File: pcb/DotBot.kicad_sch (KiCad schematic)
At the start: 65 parts, among them J1 Shield Header, J10 Extra Pins, J11 Motor connector, J12 Motor connector, J6 SWD, J7 Shield Header, J8 Extra Pins, J9 Extra Pins, Q1 DMN62D0U-7, Q2 DMG2301L-7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

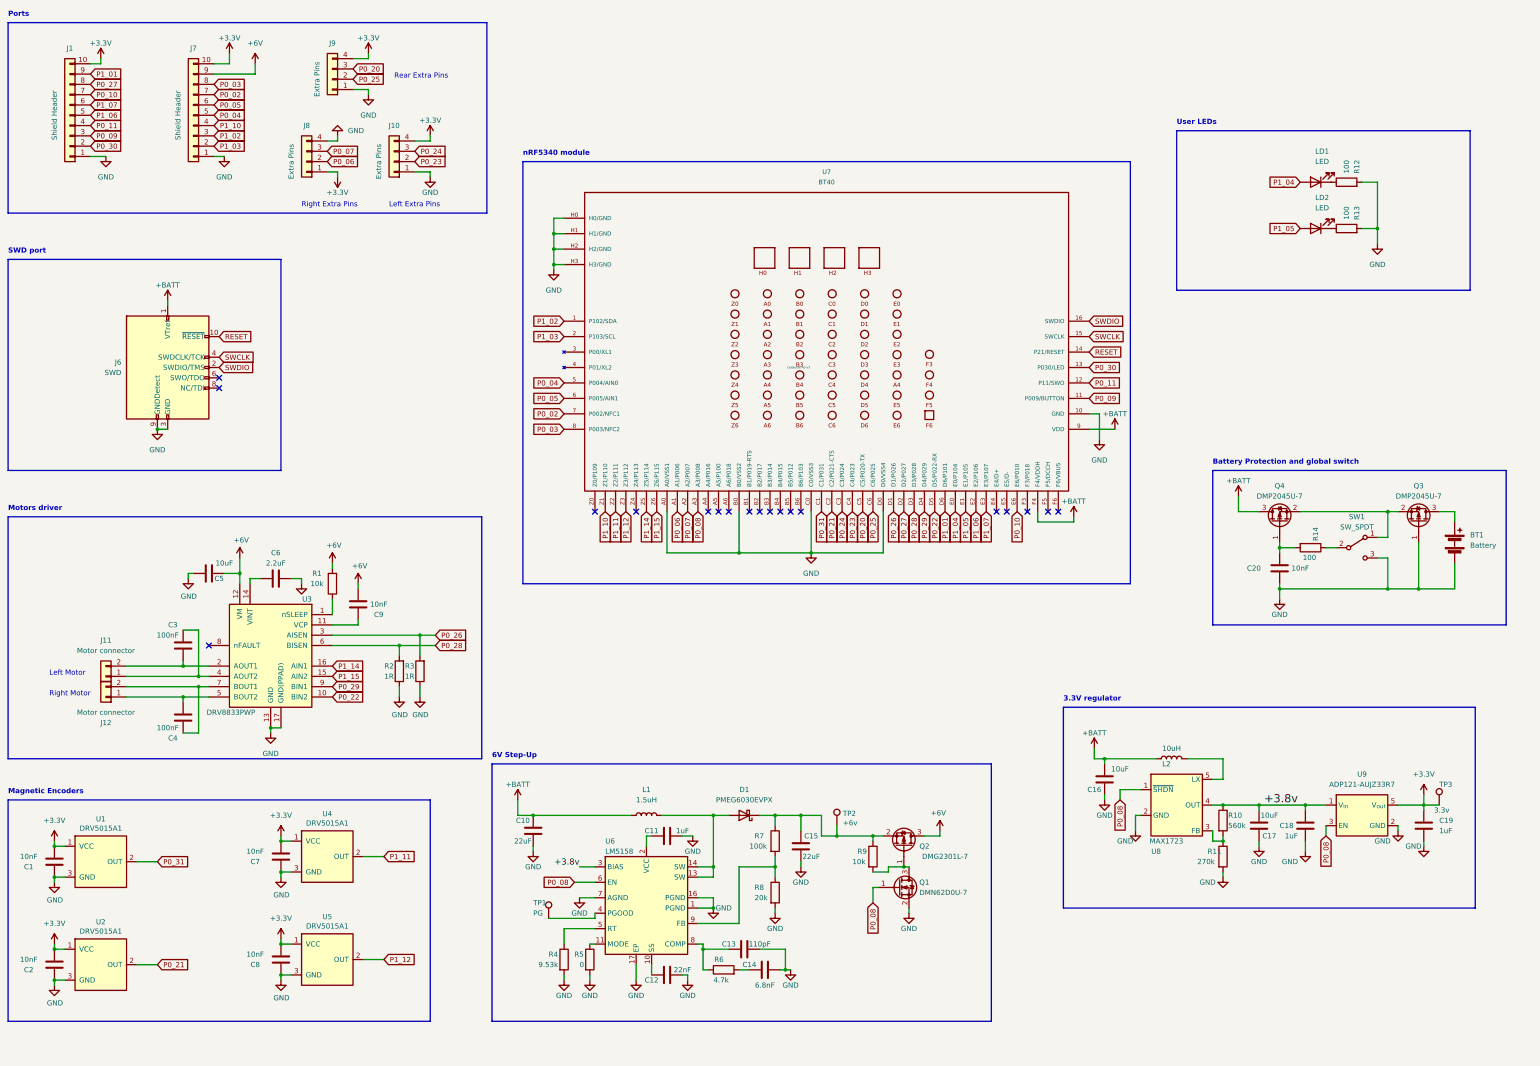
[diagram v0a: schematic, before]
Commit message: #11 3v-motor: Remove 6v step-up, replace 3.3v step-up for a 5v step-up
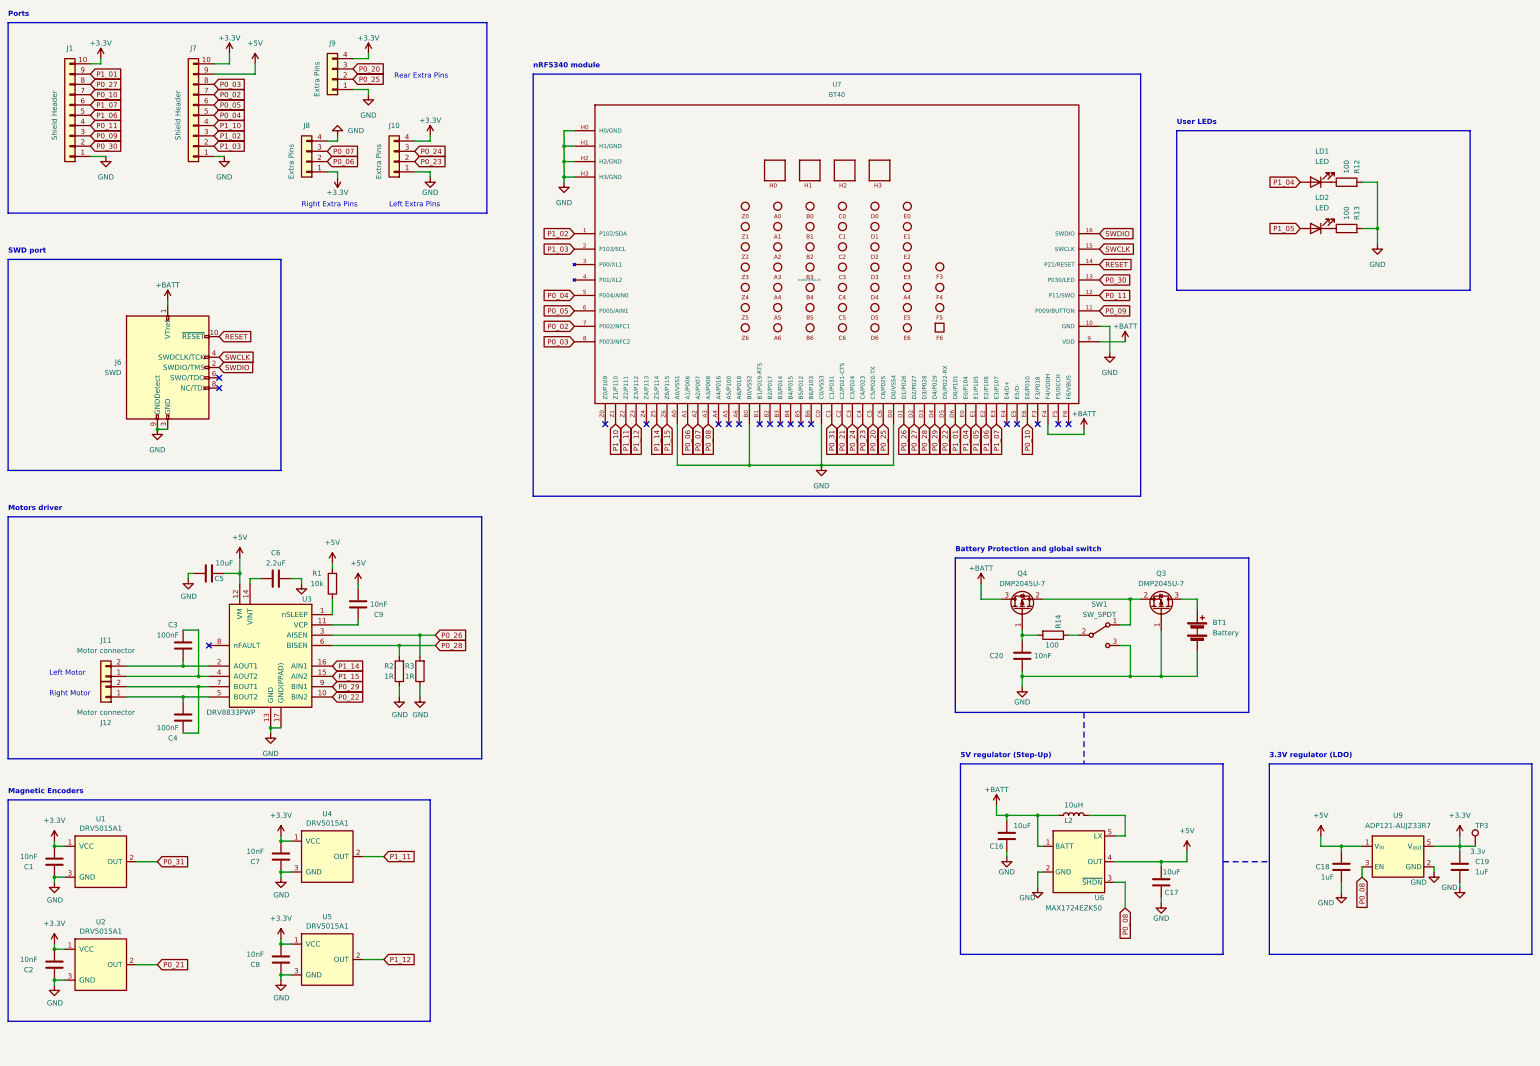
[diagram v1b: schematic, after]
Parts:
- removed C10, C15: 22uF, Capacitor_SMD:C_0805_2012Metric, symbol Device:C
- removed C11: 1uF, Capacitor_SMD:C_0603_1608Metric, symbol Device:C
- removed C12: 22nF, Capacitor_SMD:C_0603_1608Metric, symbol Device:C
- removed C13: 110pF, Capacitor_SMD:C_0603_1608Metric, symbol Device:C
- removed C14: 6.8nF, Capacitor_SMD:C_0603_1608Metric, symbol Device:C
- removed D1: PMEG6030EVPX, Diode_SMD:D_SOD-128, symbol Device:D_Schottky
- removed L1: 1.5uH, Inductor_SMD:L_1008_2520Metric, symbol Device:L
- removed Q1: DMN62D0U-7, Package_TO_SOT_SMD:SOT-23, symbol Device:Q_NMOS_GSD
- removed Q2: DMG2301L-7, Package_TO_SOT_SMD:SOT-23, symbol Device:Q_PMOS_GSD
- removed R10: 560k, Resistor_SMD:R_0603_1608Metric, symbol Device:R
- removed R11: 270k, Resistor_SMD:R_0603_1608Metric, symbol Device:R
- removed R4: 9.53k, Resistor_SMD:R_0603_1608Metric, symbol Device:R
- removed R5: 0, Resistor_SMD:R_0603_1608Metric, symbol Device:R
- removed R6: 4.7k, Resistor_SMD:R_0603_1608Metric, symbol Device:R
- removed R7: 100k, Resistor_SMD:R_0603_1608Metric, symbol Device:R
- removed R8: 20k, Resistor_SMD:R_0603_1608Metric, symbol Device:R
- removed R9: 10k, Resistor_SMD:R_0603_1608Metric, symbol Device:R
- removed TP1: PG, TestPoint:TestPoint_Pad_D1.0mm, symbol Connector:TestPoint
- removed TP2: +6v, TestPoint:TestPoint_Pad_D1.0mm, symbol Connector:TestPoint
- removed U6: LM5158, Package_DFN_QFN:WQFN-16-1EP_3x3mm_P0.5mm_EP1.6x1.6mm_ThermalVias, symbol DotBot:LM5158
- removed U8: MAX1723, Package_TO_SOT_SMD:SOT-23-5, symbol DotBot:MAX1723
- added U6: MAX1724EZK50, Package_TO_SOT_SMD:SOT-23-5, symbol DotBot:MAX1724EZK50
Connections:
- net +6V is gone; now on net +5V: C5.1, C9.1, J7.9 (Pin_9), R1.2, U3.12 (VM)
- net +BATT: now also U6.1 (BATT)
- net GND: now also U6.2 (GND)
- net P0_08: now also U6.3 (~{SHDN})
- net at L2.2: now also U6.5 (LX)
- net +3.8v renamed +5V
- net +5V: now also U6.4 (OUT)
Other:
- note added: "3.3V regulator (LDO)"
- note added: "5V regulator (Step-Up)"
- note removed: "3.3V regulator"
- note removed: "6V Step-Up"
- moved on the sheet: BT1, C16, C17, C18, C19, C20, L2, Q3, Q4, R14, SW1, TP3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

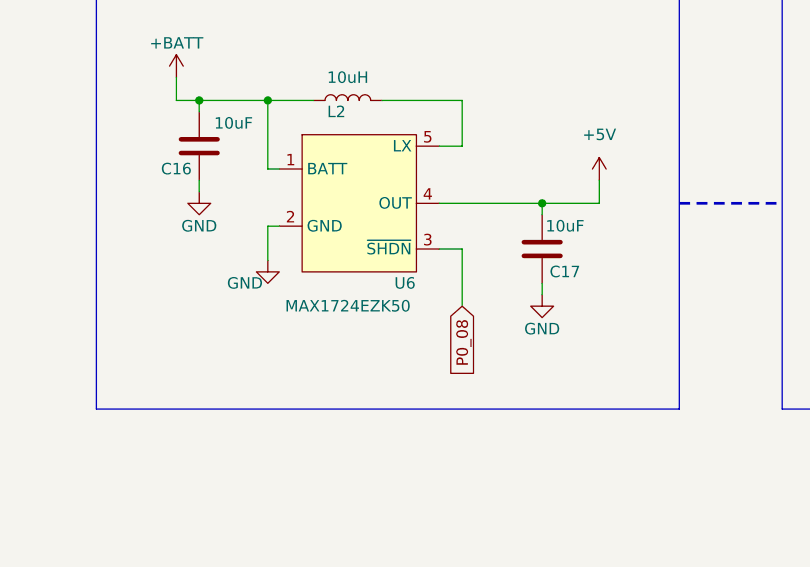
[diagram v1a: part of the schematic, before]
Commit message: #11 3v-motor: (fix) keep the U8 designator from the 3.3v reg, to the new 5v reg
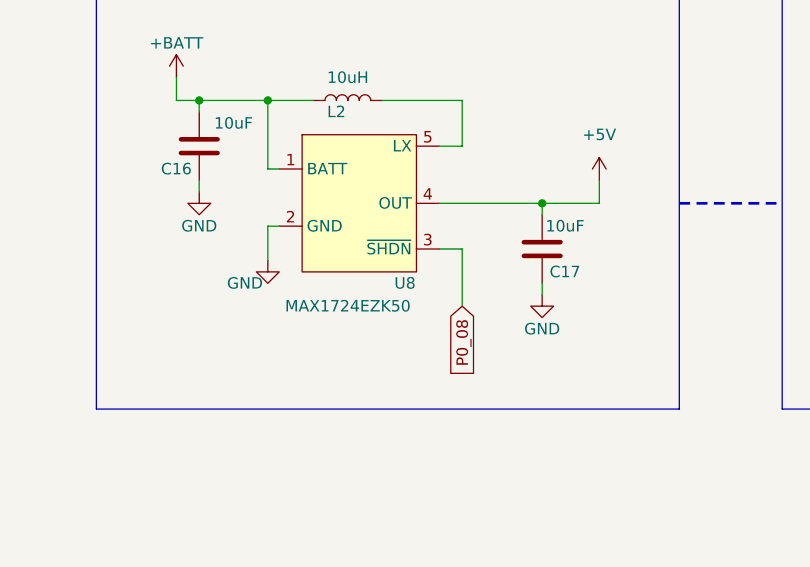
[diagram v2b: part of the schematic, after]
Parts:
- renumbered U6 to U8
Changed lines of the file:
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@@
   (symbol (lib_id "DotBot:MAX1724EZK50") (at 293.37 228.6 0) (unit 1)
     (in_bom yes) (on_board yes) (dnp no)
-    (property "Reference" "U6" (at 295.91 234.95 0)
+    (property "Reference" "U8" (at 295.91 234.95 0)
       (effects (font (size 1.27 1.27)))
     )
@@
       (project "DotBot"
         (path "/491c1a28-9007-4b9b-b900-130d9dcda097"
-          (reference "U6") (unit 1)
+          (reference "U8") (unit 1)
         )
       )

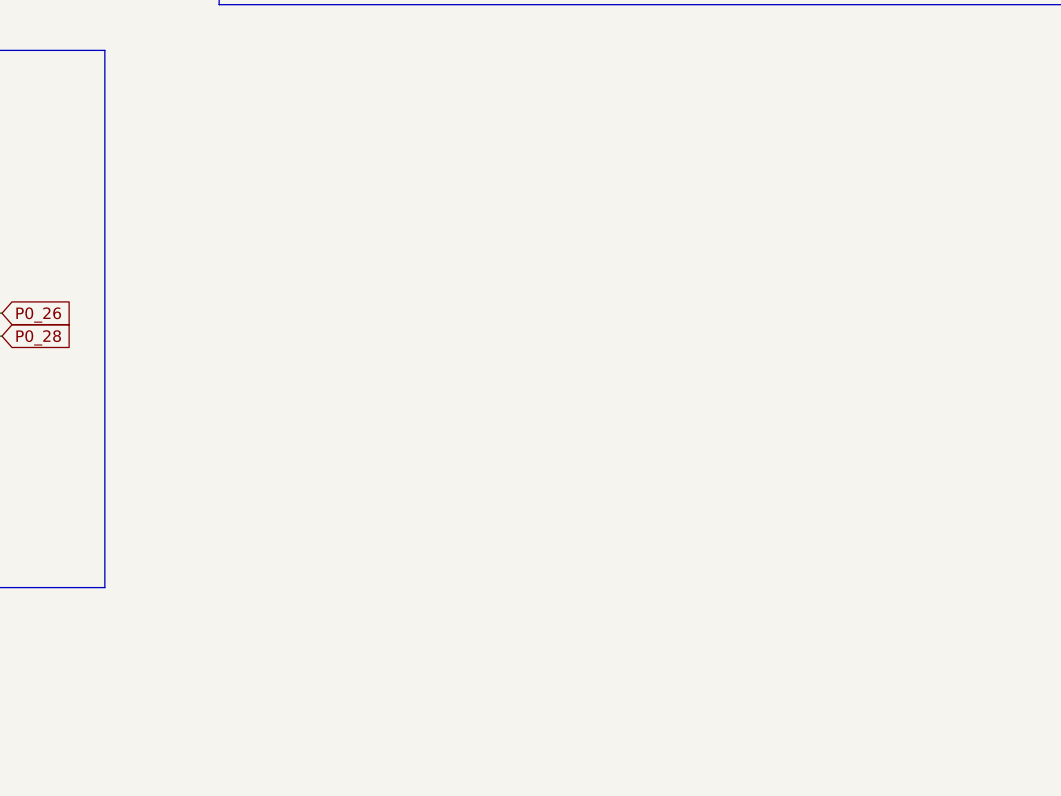
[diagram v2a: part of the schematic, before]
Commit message: #11 3v-motor: start drawing the motor driver schematic
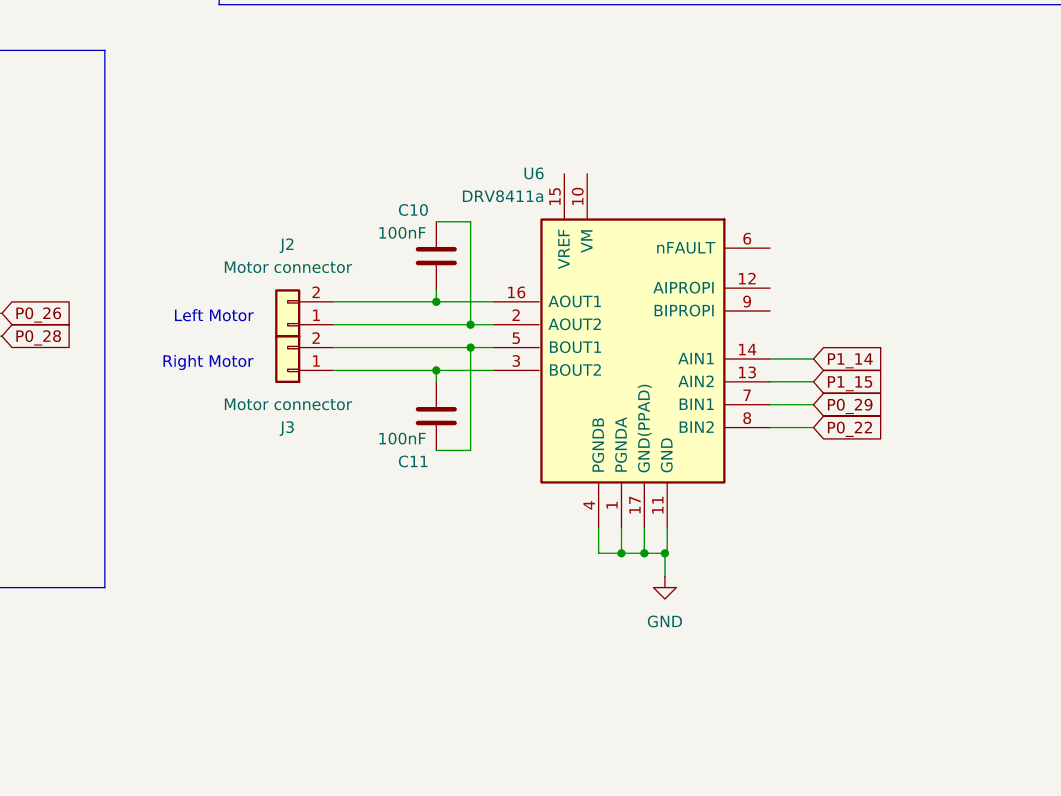
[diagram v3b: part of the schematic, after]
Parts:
- added C10, C11: 100nF, Capacitor_SMD:C_0603_1608Metric, symbol Device:C
- added J2, J3: Motor connector, Connector_JST:JST_PH_B2B-PH-K_1x02_P2.00mm_Vertical, symbol Connector_Generic:Conn_01x02
- added U6: DRV8411a, Package_SO:HTSSOP-16-1EP_4.4x5mm_P0.65mm_EP3.4x5mm_Mask2.46x2.31mm_ThermalVias, symbol DotBot:DRV8411a
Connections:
- net GND: now also U6.1 (PGNDA), U6.11 (GND), U6.17 (GND(PPAD)), U6.4 (PGNDB)
- net P0_22: now also U6.8 (BIN2)
- net P0_29: now also U6.7 (BIN1)
- net P1_14: now also U6.14 (AIN1)
- net P1_15: now also U6.13 (AIN2)
- new net: C11.1, J3.1 (Pin_1), U6.3 (BOUT2)
- new net: C11.2, J3.2 (Pin_2), U6.5 (BOUT1)
- new net: C10.2, J2.2 (Pin_2), U6.16 (AOUT1)
- new net: C10.1, J2.1 (Pin_1), U6.2 (AOUT2)

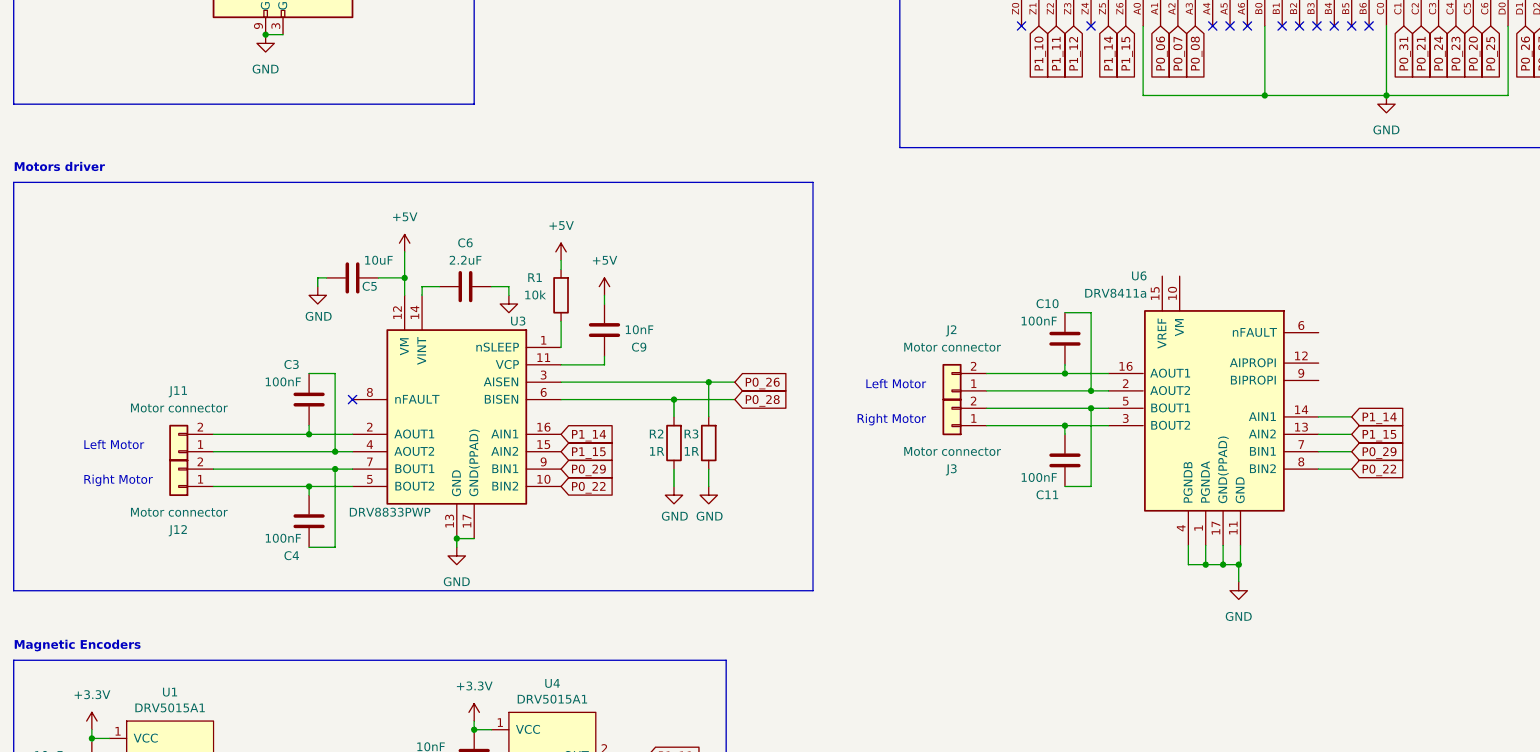
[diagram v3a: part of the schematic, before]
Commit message: #11 3v-motor: add new motor driver to schematic
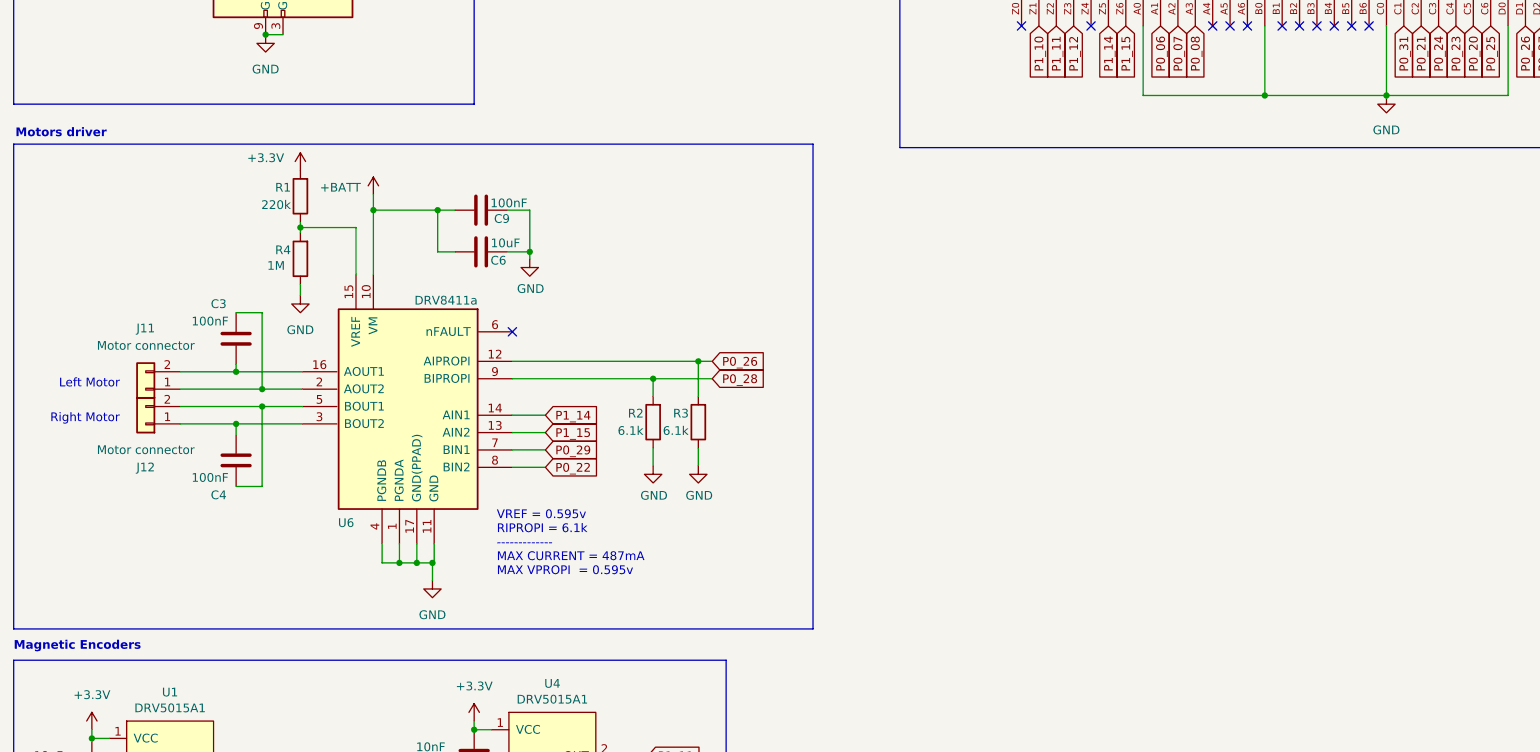
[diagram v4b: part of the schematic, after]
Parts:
- removed C3, C4: 100nF, Capacitor_SMD:C_0603_1608Metric, symbol Device:C
- removed C6: 2.2uF, Capacitor_SMD:C_0603_1608Metric, symbol Device:C
- removed J11, J12: Motor connector, Connector_JST:JST_PH_B2B-PH-K_1x02_P2.00mm_Vertical, symbol Connector_Generic:Conn_01x02
- removed U3: DRV8833PWP, Package_SO:HTSSOP-16-1EP_4.4x5mm_P0.65mm_EP3.4x5mm_Mask2.46x2.31mm_ThermalVias, symbol Driver_Motor:DRV8833PWP
- added R4: 1M, Resistor_SMD:R_0603_1608Metric, symbol Device:R
- C9: value 10nF -> 100nF
- R1: value 10k -> 220k; Link https://www.digikey.com/short/f8zjrt52 -> https://www.digikey.com/short/vj5058q2; Mfr Part Number RC0603FR-0710KL -> RC0603FR-071RL; Price 0.0043 -> 0.0087
- R2, R3: value 1R -> 6.1k
- renumbered C10 to C3, C11 to C4, C5 to C6, J2 to J11, J3 to J12
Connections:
- net +3V3: now also R1.2
- net +5V: no longer C6.1, C9.1, R1.2
- net +BATT: now also C6.2, C9.1, U6.10 (VM)
- net GND: now also C6.1, C9.2, R4.1; no longer C6.2
- net P0_26: now also U6.12 (AIPROPI)
- net P0_28: now also U6.9 (BIPROPI)
- net at R1.1: now also U6.15 (VREF), R4.2
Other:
- note added: "VREF = 0.595v RIPROPI = 6.1k ------------- MAX CURRENT = 487mA MAX VPROPI = 0.595v"
- moved on the sheet: C3, C4, C6, J11, J12, U6
